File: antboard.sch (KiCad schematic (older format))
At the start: 0 parts

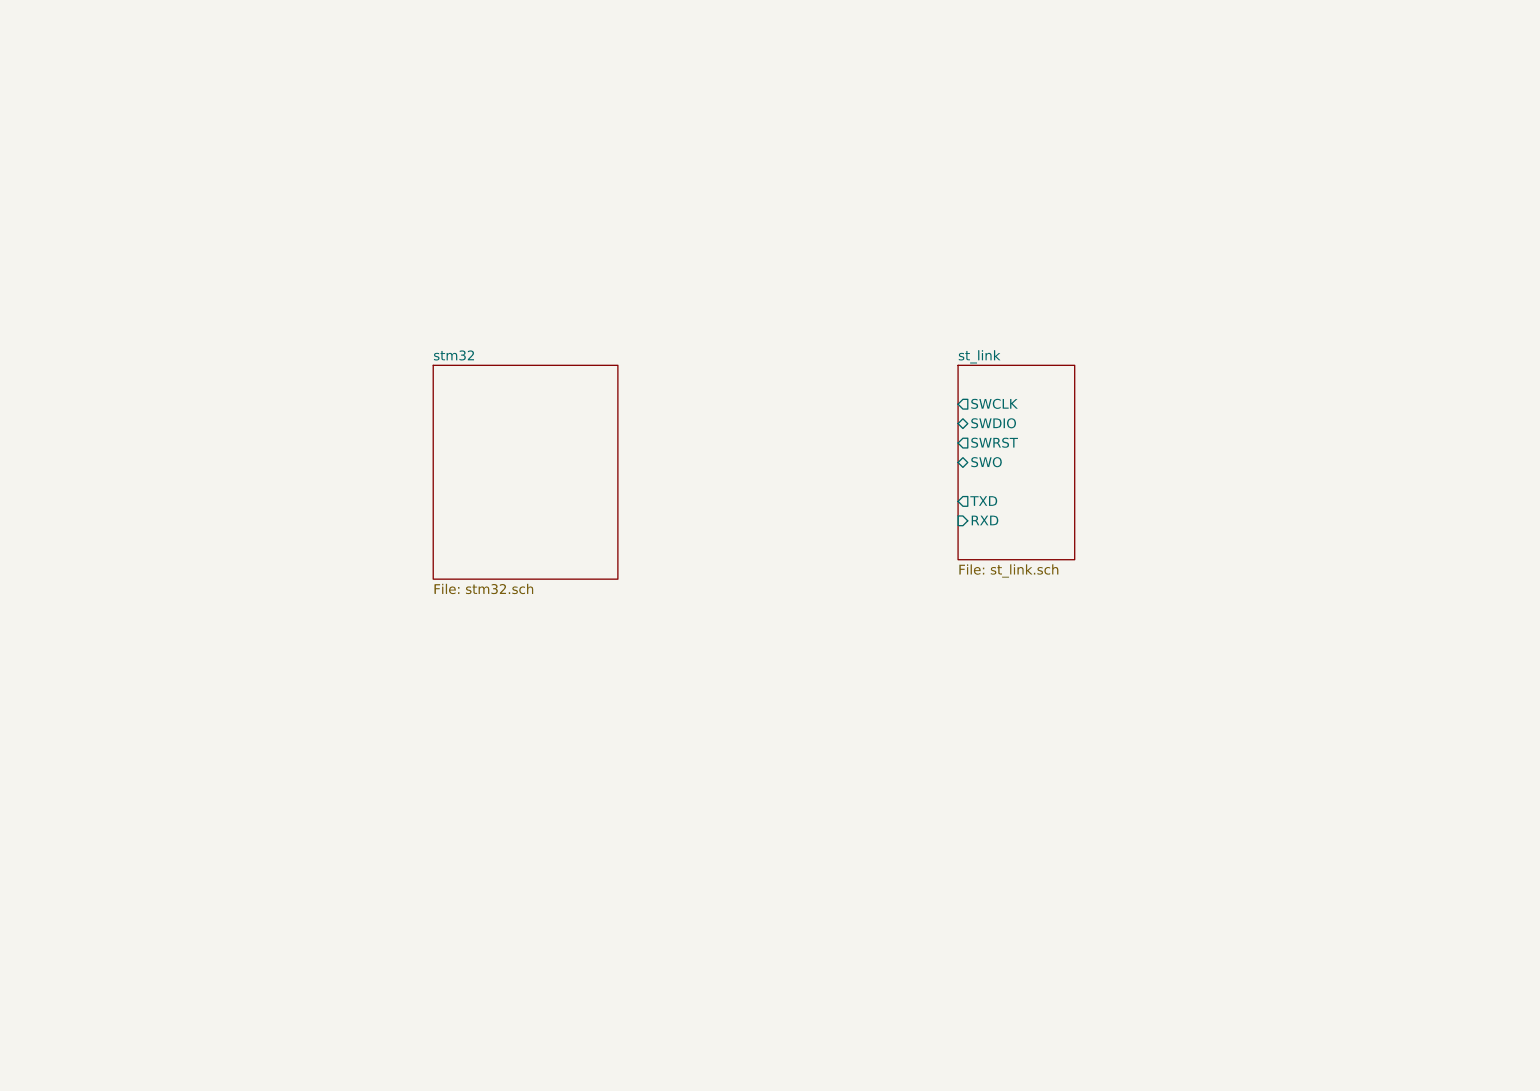
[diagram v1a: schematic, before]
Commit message: Better sch segmentation and add TCA6424A symbol
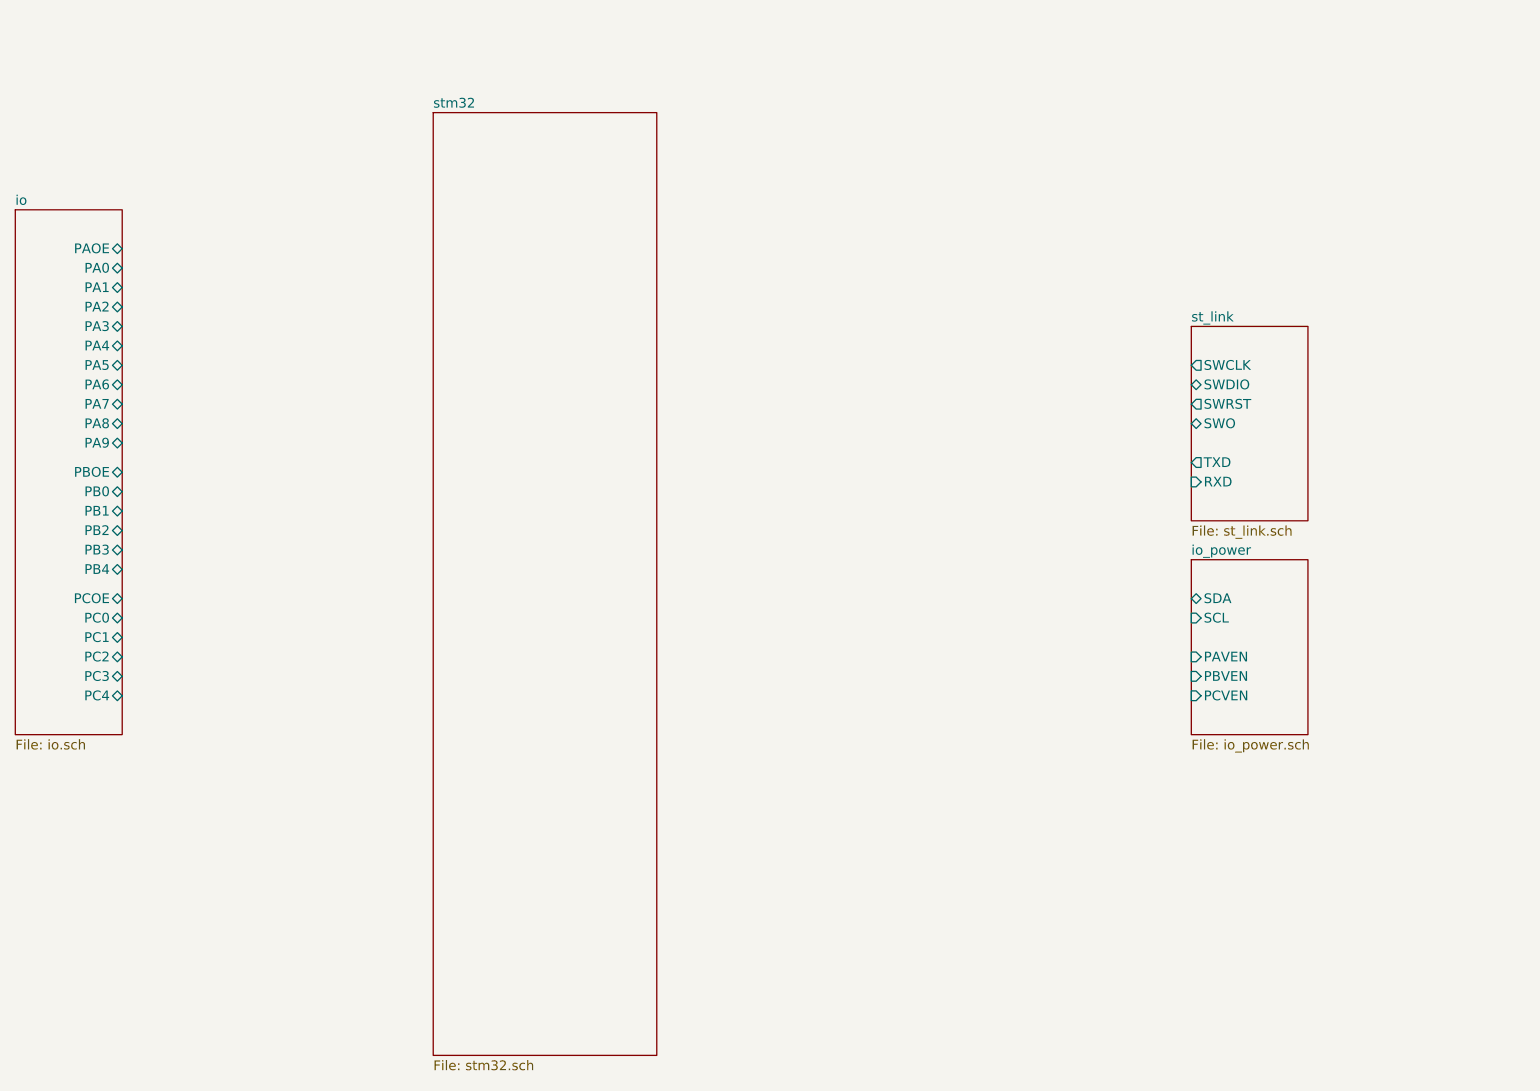
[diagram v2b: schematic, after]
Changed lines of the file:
@@
 $Descr A4 11693 8268
 encoding utf-8
-Sheet 1 3
+Sheet 1 5
 Title "STM32 devboard with .05\" headers"
 Date "2019-11-26"
@@
 $EndDescr
 $Sheet
-S 5950 2800 600  1000
+S 7150 2600 600  1000
 U 5DF7E971
 F0 "st_link" 50
 F1 "st_link.sch" 50
-F2 "SWCLK" O L 5950 3000 50
-F3 "SWDIO" B L 5950 3100 50
-F4 "SWRST" O L 5950 3200 50
-F5 "SWO" B L 5950 3300 50
-F6 "TXD" O L 5950 3500 50
-F7 "RXD" I L 5950 3600 50
+F2 "SWCLK" O L 7150 2800 50
+F3 "SWDIO" B L 7150 2900 50
+F4 "SWRST" O L 7150 3000 50
+F5 "SWO" B L 7150 3100 50
+F6 "TXD" O L 7150 3300 50
+F7 "RXD" I L 7150 3400 50
 $EndSheet
 $Sheet
-S 3250 2800 950  1100
+S 3250 1500 1150 4850
 U 5DFC2583
 F0 "stm32" 50
 F1 "stm32.sch" 50
 $EndSheet
+$Sheet
+S 1100 2000 550  2700
+U 5E933CA7
+F0 "io" 50
+F1 "io.sch" 50
+F2 "PAOE" B R 1650 2200 50
+F3 "PA0" B R 1650 2300 50
+F4 "PA1" B R 1650 2400 50
+F5 "PA2" B R 1650 2500 50
+F6 "PA3" B R 1650 2600 50
+F7 "PA4" B R 1650 2700 50
+F8 "PA5" B R 1650 2800 50
+F9 "PA6" B R 1650 2900 50
+F10 "PA7" B R 1650 3000 50
+F11 "PA8" B R 1650 3100 50
+F12 "PA9" B R 1650 3200 50
+F13 "PBOE" B R 1650 3350 50
+F14 "PB0" B R 1650 3450 50
+F15 "PB1" B R 1650 3550 50
+F16 "PB2" B R 1650 3650 50
+F17 "PB3" B R 1650 3750 50
+F18 "PB4" B R 1650 3850 50
+F19 "PCOE" B R 1650 4000 50
+F20 "PC0" B R 1650 4100 50
+F21 "PC1" B R 1650 4200 50
+F22 "PC2" B R 1650 4300 50
+F23 "PC3" B R 1650 4400 50
+F24 "PC4" B R 1650 4500 50
+$EndSheet
+$Sheet
+S 7150 3800 600  900
+U 5EA8F1AB
+F0 "io_power" 50
+F1 "io_power.sch" 50
+F2 "SDA" B L 7150 4000 50
+F3 "SCL" I L 7150 4100 50
+F4 "PAVEN" I L 7150 4300 50
+F5 "PBVEN" I L 7150 4400 50
+F6 "PCVEN" I L 7150 4500 50
+$EndSheet
 $EndSCHEMATC

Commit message: Done adding the kitchen sink
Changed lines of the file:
@@
 EESchema Schematic File Version 4
-LIBS:antboard-cache
 EELAYER 30 0
 EELAYER END
@@
 $EndDescr
 $Sheet
-S 7150 2600 600  1000
+S 8000 2550 600  1000
 U 5DF7E971
 F0 "st_link" 50
 F1 "st_link.sch" 50
-F2 "SWCLK" O L 7150 2800 50
-F3 "SWDIO" B L 7150 2900 50
-F4 "SWRST" O L 7150 3000 50
-F5 "SWO" B L 7150 3100 50
-F6 "TXD" O L 7150 3300 50
-F7 "RXD" I L 7150 3400 50
+F2 "SWCLK" O L 8000 2750 50
+F3 "SWDIO" B L 8000 2850 50
+F4 "SWRST" O L 8000 2950 50
+F5 "SWO" B L 8000 3050 50
+F6 "TXD" O L 8000 3250 50
+F7 "RXD" I L 8000 3350 50
 $EndSheet
 $Sheet
-S 3250 1500 1150 4850
+S 4700 1100 1150 4850
 U 5DFC2583
 F0 "stm32" 50
@@
 $EndSheet
 $Sheet
-S 1100 2000 550  2700
+S 1950 1950 550  2700
 U 5E933CA7
 F0 "io" 50
 F1 "io.sch" 50
-F2 "PAOE" B R 1650 2200 50
-F3 "PA0" B R 1650 2300 50
-F4 "PA1" B R 1650 2400 50
-F5 "PA2" B R 1650 2500 50
-F6 "PA3" B R 1650 2600 50
-F7 "PA4" B R 1650 2700 50
-F8 "PA5" B R 1650 2800 50
-F9 "PA6" B R 1650 2900 50
-F10 "PA7" B R 1650 3000 50
-F11 "PA8" B R 1650 3100 50
-F12 "PA9" B R 1650 3200 50
-F13 "PBOE" B R 1650 3350 50
-F14 "PB0" B R 1650 3450 50
-F15 "PB1" B R 1650 3550 50
-F16 "PB2" B R 1650 3650 50
-F17 "PB3" B R 1650 3750 50
-F18 "PB4" B R 1650 3850 50
-F19 "PCOE" B R 1650 4000 50
-F20 "PC0" B R 1650 4100 50
-F21 "PC1" B R 1650 4200 50
-F22 "PC2" B R 1650 4300 50
-F23 "PC3" B R 1650 4400 50
-F24 "PC4" B R 1650 4500 50
+F2 "PAOE" B R 2500 2150 50
+F3 "PA0" B R 2500 2250 50
+F4 "PA1" B R 2500 2350 50
+F5 "PA2" B R 2500 2450 50
+F6 "PA3" B R 2500 2550 50
+F7 "PA4" B R 2500 2650 50
+F8 "PA5" B R 2500 2750 50
+F9 "PA6" B R 2500 2850 50
+F10 "PA7" B R 2500 2950 50
+F11 "PA8" B R 2500 3050 50
+F12 "PA9" B R 2500 3150 50
+F13 "PBOE" B R 2500 3300 50
+F14 "PB0" B R 2500 3400 50
+F15 "PB1" B R 2500 3500 50
+F16 "PB2" B R 2500 3600 50
+F17 "PB3" B R 2500 3700 50
+F18 "PB4" B R 2500 3800 50
+F19 "PCOE" B R 2500 3950 50
+F20 "PC0" B R 2500 4050 50
+F21 "PC1" B R 2500 4150 50
+F22 "PC2" B R 2500 4250 50
+F23 "PC3" B R 2500 4350 50
+F24 "PC4" B R 2500 4450 50
 $EndSheet
 $Sheet
-S 7150 3800 600  900
+S 8000 3750 600  900
 U 5EA8F1AB
 F0 "io_power" 50
 F1 "io_power.sch" 50
-F2 "SDA" B L 7150 4000 50
-F3 "SCL" I L 7150 4100 50
-F4 "PAVEN" I L 7150 4300 50
-F5 "PBVEN" I L 7150 4400 50
-F6 "PCVEN" I L 7150 4500 50
+F2 "SDA" B L 8000 3950 50
+F3 "SCL" I L 8000 4050 50
+F4 "PAVEN" I L 8000 4250 50
+F5 "PBVEN" I L 8000 4350 50
+F6 "PCVEN" I L 8000 4450 50
 $EndSheet
 $EndSCHEMATC

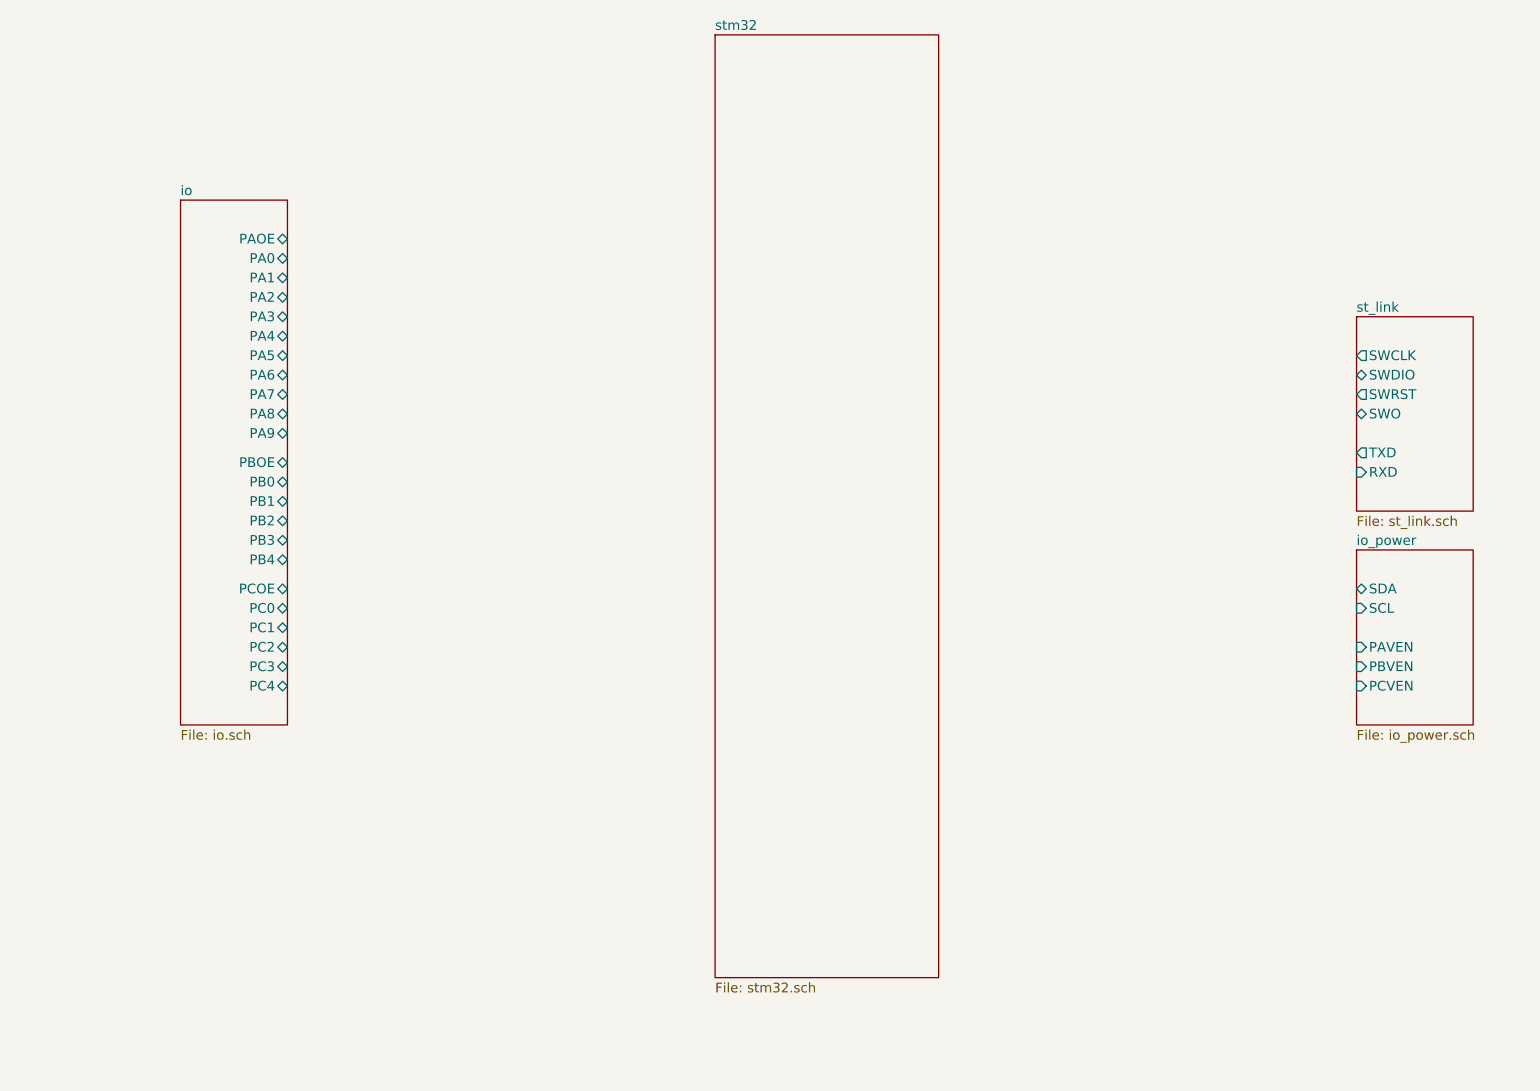
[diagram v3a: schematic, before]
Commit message: Schematic mostly done, place begun
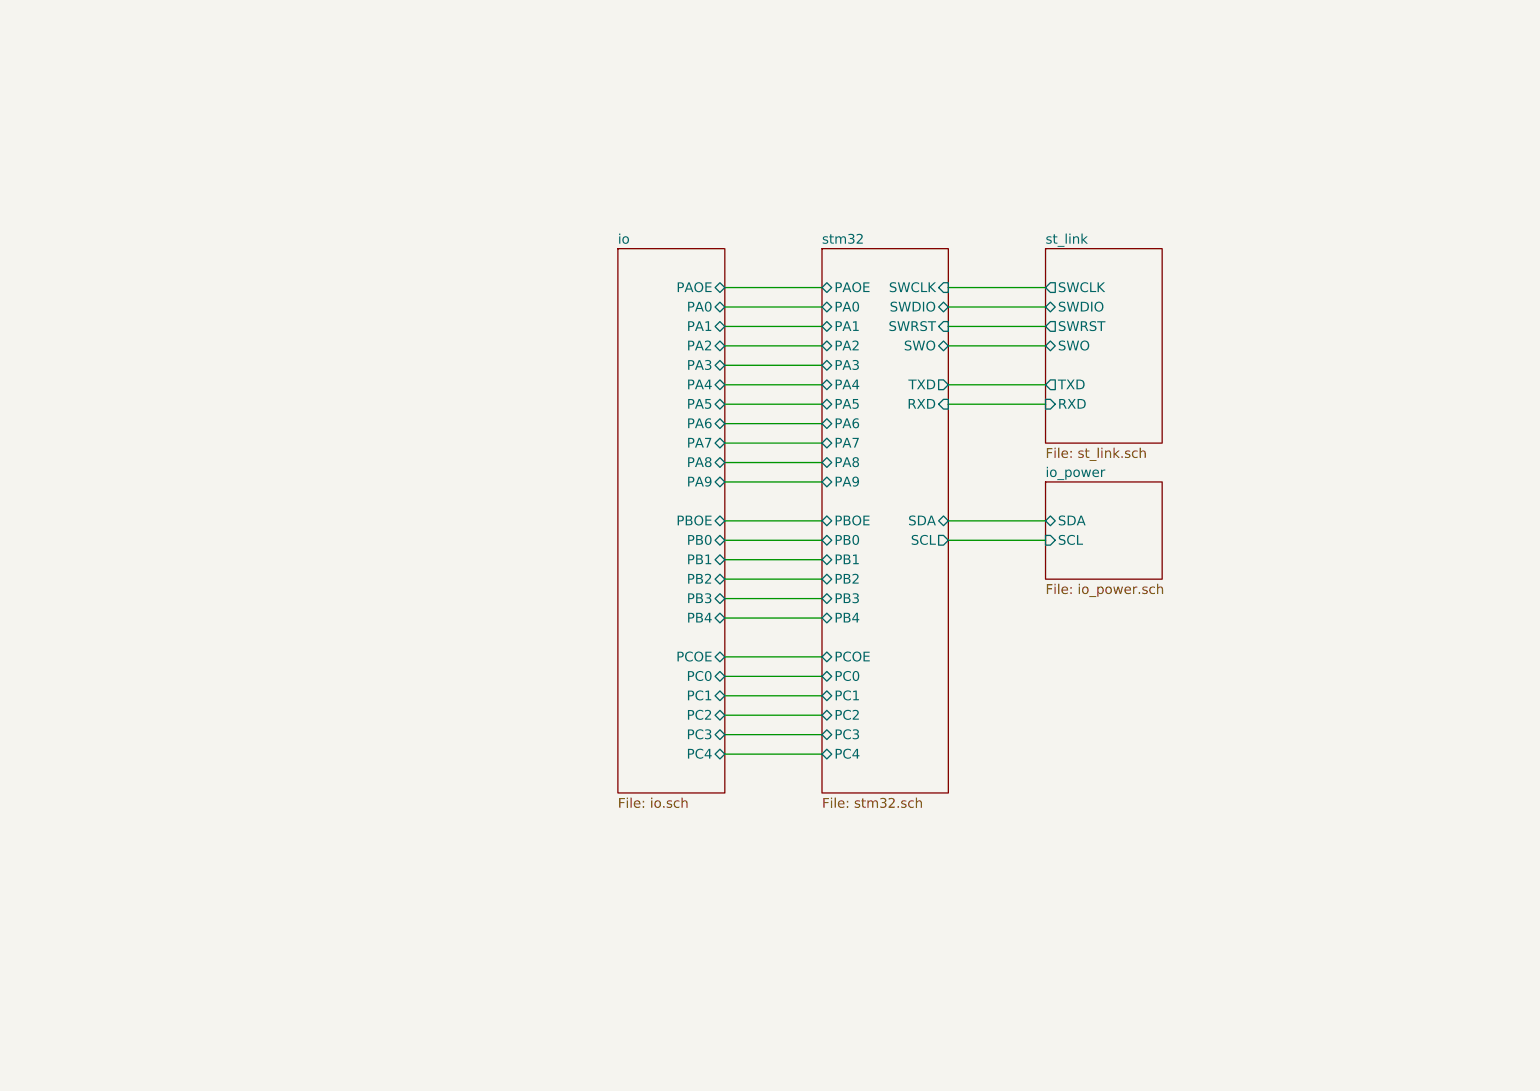
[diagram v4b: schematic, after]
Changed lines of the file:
@@
 $EndDescr
 $Sheet
-S 8000 2550 600  1000
+S 6400 2200 600  1000
 U 5DF7E971
 F0 "st_link" 50
 F1 "st_link.sch" 50
-F2 "SWCLK" O L 8000 2750 50
-F3 "SWDIO" B L 8000 2850 50
-F4 "SWRST" O L 8000 2950 50
-F5 "SWO" B L 8000 3050 50
-F6 "TXD" O L 8000 3250 50
-F7 "RXD" I L 8000 3350 50
+F2 "SWCLK" O L 6400 2400 50
+F3 "SWDIO" B L 6400 2500 50
+F4 "SWRST" O L 6400 2600 50
+F5 "SWO" B L 6400 2700 50
+F6 "TXD" O L 6400 2900 50
+F7 "RXD" I L 6400 3000 50
 $EndSheet
 $Sheet
-S 4700 1100 1150 4850
+S 5250 2200 650  2800
 U 5DFC2583
 F0 "stm32" 50
 F1 "stm32.sch" 50
+F2 "SWCLK" I R 5900 2400 50
+F3 "SWDIO" B R 5900 2500 50
+F4 "SWRST" I R 5900 2600 50
+F5 "SWO" B R 5900 2700 50
+F6 "TXD" O R 5900 2900 50
+F7 "RXD" I R 5900 3000 50
+F8 "PAOE" B L 5250 2400 50
+F9 "PA0" B L 5250 2500 50
+F10 "PA1" B L 5250 2600 50
+F11 "PA2" B L 5250 2700 50
+F12 "PA3" B L 5250 2800 50
+F13 "PA4" B L 5250 2900 50
+F14 "PA5" B L 5250 3000 50
+F15 "PA6" B L 5250 3100 50
+F16 "PA7" B L 5250 3200 50
+F17 "PA9" B L 5250 3400 50
+F18 "PA8" B L 5250 3300 50
+F19 "PBOE" B L 5250 3600 50
+F20 "PB0" B L 5250 3700 50
+F21 "PB1" B L 5250 3800 50
+F22 "PB2" B L 5250 3900 50
+F23 "PB3" B L 5250 4000 50
+F24 "PB4" B L 5250 4100 50
+F25 "PCOE" B L 5250 4300 50
+F26 "PC0" B L 5250 4400 50
+F27 "PC1" B L 5250 4500 50
+F28 "PC2" B L 5250 4600 50
+F29 "PC3" B L 5250 4700 50
+F30 "PC4" B L 5250 4800 50
+F31 "SDA" B R 5900 3600 50
+F32 "SCL" O R 5900 3700 50
 $EndSheet
 $Sheet
-S 1950 1950 550  2700
+S 4200 2200 550  2800
 U 5E933CA7
 F0 "io" 50
 F1 "io.sch" 50
-F2 "PAOE" B R 2500 2150 50
-F3 "PA0" B R 2500 2250 50
-F4 "PA1" B R 2500 2350 50
-F5 "PA2" B R 2500 2450 50
-F6 "PA3" B R 2500 2550 50
-F7 "PA4" B R 2500 2650 50
-F8 "PA5" B R 2500 2750 50
-F9 "PA6" B R 2500 2850 50
-F10 "PA7" B R 2500 2950 50
-F11 "PA8" B R 2500 3050 50
-F12 "PA9" B R 2500 3150 50
-F13 "PBOE" B R 2500 3300 50
-F14 "PB0" B R 2500 3400 50
-F15 "PB1" B R 2500 3500 50
-F16 "PB2" B R 2500 3600 50
-F17 "PB3" B R 2500 3700 50
-F18 "PB4" B R 2500 3800 50
-F19 "PCOE" B R 2500 3950 50
-F20 "PC0" B R 2500 4050 50
-F21 "PC1" B R 2500 4150 50
-F22 "PC2" B R 2500 4250 50
-F23 "PC3" B R 2500 4350 50
-F24 "PC4" B R 2500 4450 50
+F2 "PAOE" B R 4750 2400 50
+F3 "PA0" B R 4750 2500 50
+F4 "PA1" B R 4750 2600 50
+F5 "PA2" B R 4750 2700 50
+F6 "PA3" B R 4750 2800 50
+F7 "PA4" B R 4750 2900 50
+F8 "PA5" B R 4750 3000 50
+F9 "PA6" B R 4750 3100 50
+F10 "PA7" B R 4750 3200 50
+F11 "PA8" B R 4750 3300 50
+F12 "PA9" B R 4750 3400 50
+F13 "PBOE" B R 4750 3600 50
+F14 "PB0" B R 4750 3700 50
+F15 "PB1" B R 4750 3800 50
+F16 "PB2" B R 4750 3900 50
+F17 "PB3" B R 4750 4000 50
+F18 "PB4" B R 4750 4100 50
+F19 "PCOE" B R 4750 4300 50
+F20 "PC0" B R 4750 4400 50
+F21 "PC1" B R 4750 4500 50
+F22 "PC2" B R 4750 4600 50
+F23 "PC3" B R 4750 4700 50
+F24 "PC4" B R 4750 4800 50
 $EndSheet
 $Sheet
-S 8000 3750 600  900
+S 6400 3400 600  500
 U 5EA8F1AB
 F0 "io_power" 50
 F1 "io_power.sch" 50
-F2 "SDA" B L 8000 3950 50
-F3 "SCL" I L 8000 4050 50
-F4 "PAVEN" I L 8000 4250 50
-F5 "PBVEN" I L 8000 4350 50
-F6 "PCVEN" I L 8000 4450 50
+F2 "SDA" B L 6400 3600 50
+F3 "SCL" I L 6400 3700 50
 $EndSheet
+Wire Wire Line
+	4750 2400 5250 2400
+Wire Wire Line
+	5250 2500 4750 2500
+Wire Wire Line
+	4750 2600 5250 2600
+Wire Wire Line
+	5250 2700 4750 2700
+Wire Wire Line
+	4750 2800 5250 2800
+Wire Wire Line
+	5250 2900 4750 2900
+Wire Wire Line
+	4750 3000 5250 3000
+Wire Wire Line
+	5250 3100 4750 3100
+Wire Wire Line
+	4750 3200 5250 3200
+Wire Wire Line
+	5250 3300 4750 3300
+Wire Wire Line
+	4750 3400 5250 3400
+Wire Wire Line
+	5250 3600 4750 3600
+Wire Wire Line
+	4750 3700 5250 3700
+Wire Wire Line
+	5250 3800 4750 3800
+Wire Wire Line
+	4750 3900 5250 3900
+Wire Wire Line
+	5250 4000 4750 4000
+Wire Wire Line
+	4750 4100 5250 4100
+Wire Wire Line
+	5250 4500 4750 4500
+Wire Wire Line
+	4750 4300 5250 4300
+Wire Wire Line
+	5250 4400 4750 4400
+Wire Wire Line
+	4750 4600 5250 4600
+Wire Wire Line
+	5250 4700 4750 4700
+Wire Wire Line
+	4750 4800 5250 4800
+Wire Wire Line
+	5900 2400 6400 2400
+Wire Wire Line
+	6400 2500 5900 2500
+Wire Wire Line
+	5900 2600 6400 2600
+Wire Wire Line
+	6400 2700 5900 2700
+Wire Wire Line
+	5900 2900 6400 2900
+Wire Wire Line
+	6400 3000 5900 3000
+Wire Wire Line
+	5900 3600 6400 3600
+Wire Wire Line
+	6400 3700 5900 3700
 $EndSCHEMATC
